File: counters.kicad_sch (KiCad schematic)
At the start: 20 parts, among them K15 Fujitsu_FTR-LYAA005x, K17 Relay_SPDT, Q293 DMP3099L, Q294 DMP3099L, Q869 2N7002, Q871 2N7002, SW1 SW_Push, SW2 SW_Push

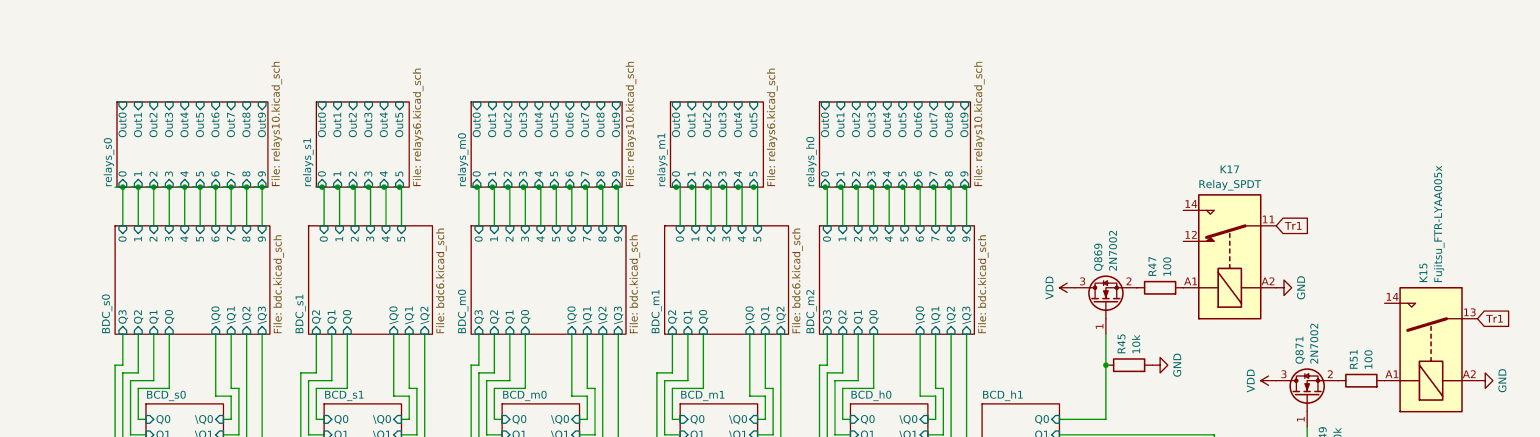
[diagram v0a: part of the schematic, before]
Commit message: moved to 3v3
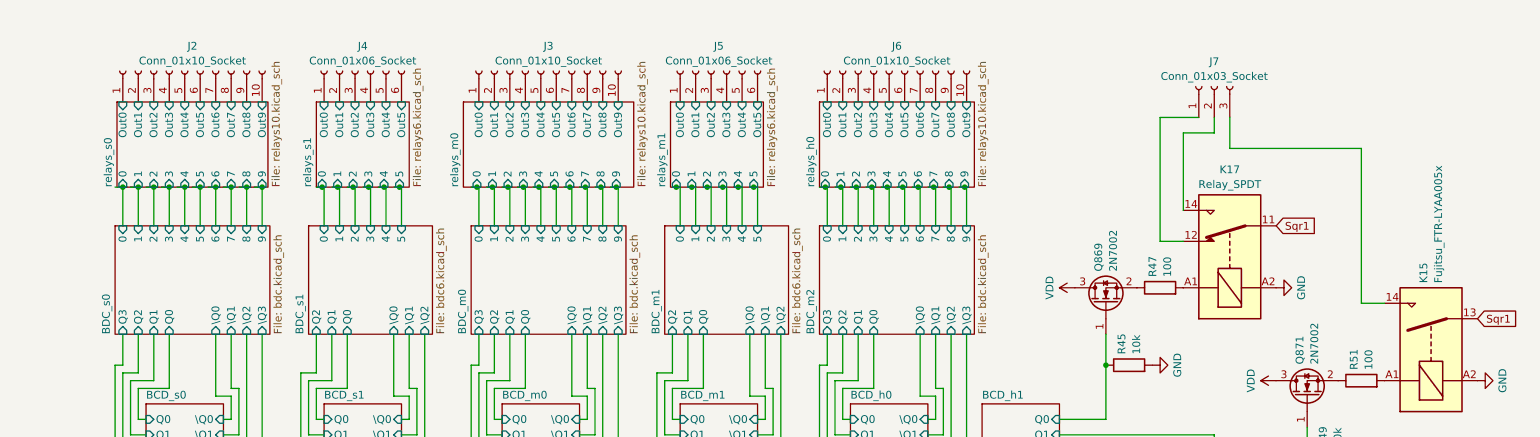
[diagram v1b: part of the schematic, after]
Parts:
- added J2, J3, J6: Conn_01x10_Socket, symbol Connector:Conn_01x10_Socket
- added J4, J5: Conn_01x06_Socket, symbol Connector:Conn_01x06_Socket
- added J7: Conn_01x03_Socket, symbol Connector:Conn_01x03_Socket
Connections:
- net relays_h0/Out0: now also J6.1 (Pin_1)
- net relays_h0/Out1: now also J6.2 (Pin_2)
- net relays_h0/Out2: now also J6.3 (Pin_3)
- net relays_h0/Out3: now also J6.4 (Pin_4)
- net relays_h0/Out4: now also J6.5 (Pin_5)
- net relays_h0/Out5: now also J6.6 (Pin_6)
- net relays_h0/Out6: now also J6.7 (Pin_7)
- net relays_h0/Out7: now also J6.8 (Pin_8)
- net relays_h0/Out8: now also J6.9 (Pin_9)
- net relays_h0/Out9: now also J6.10 (Pin_10)
- net relays_m0/Out0: now also J3.1 (Pin_1)
- net relays_m0/Out1: now also J3.2 (Pin_2)
- net relays_m0/Out2: now also J3.3 (Pin_3)
- net relays_m0/Out3: now also J3.4 (Pin_4)
- net relays_m0/Out4: now also J3.5 (Pin_5)
- net relays_m0/Out5: now also J3.6 (Pin_6)
- net relays_m0/Out6: now also J3.7 (Pin_7)
- net relays_m0/Out7: now also J3.8 (Pin_8)
- net relays_m0/Out8: now also J3.9 (Pin_9)
- net relays_m0/Out9: now also J3.10 (Pin_10)
- net relays_m1/Out0: now also J5.1 (Pin_1)
- net relays_m1/Out1: now also J5.2 (Pin_2)
- net relays_m1/Out2: now also J5.3 (Pin_3)
- net relays_m1/Out3: now also J5.4 (Pin_4)
- net relays_m1/Out4: now also J5.5 (Pin_5)
- net relays_m1/Out5: now also J5.6 (Pin_6)
- net relays_s0/Out0: now also J2.1 (Pin_1)
- net relays_s0/Out1: now also J2.2 (Pin_2)
- net relays_s0/Out2: now also J2.3 (Pin_3)
- net relays_s0/Out3: now also J2.4 (Pin_4)
- net relays_s0/Out4: now also J2.5 (Pin_5)
- net relays_s0/Out5: now also J2.6 (Pin_6)
- net relays_s0/Out6: now also J2.7 (Pin_7)
- net relays_s0/Out7: now also J2.8 (Pin_8)
- net relays_s0/Out8: now also J2.9 (Pin_9)
- net relays_s0/Out9: now also J2.10 (Pin_10)
- net relays_s1/Out0: now also J4.1 (Pin_1)
- net relays_s1/Out1: now also J4.2 (Pin_2)
- net relays_s1/Out2: now also J4.3 (Pin_3)
- net relays_s1/Out3: now also J4.4 (Pin_4)
- net relays_s1/Out4: now also J4.5 (Pin_5)
- net relays_s1/Out5: now also J4.6 (Pin_6)
- net at K15.14: now also J7.3 (Pin_3)
- net at K17.12: now also J7.1 (Pin_1)
- net at K17.14: now also J7.2 (Pin_2)
- net Tr1 renamed Sqr1

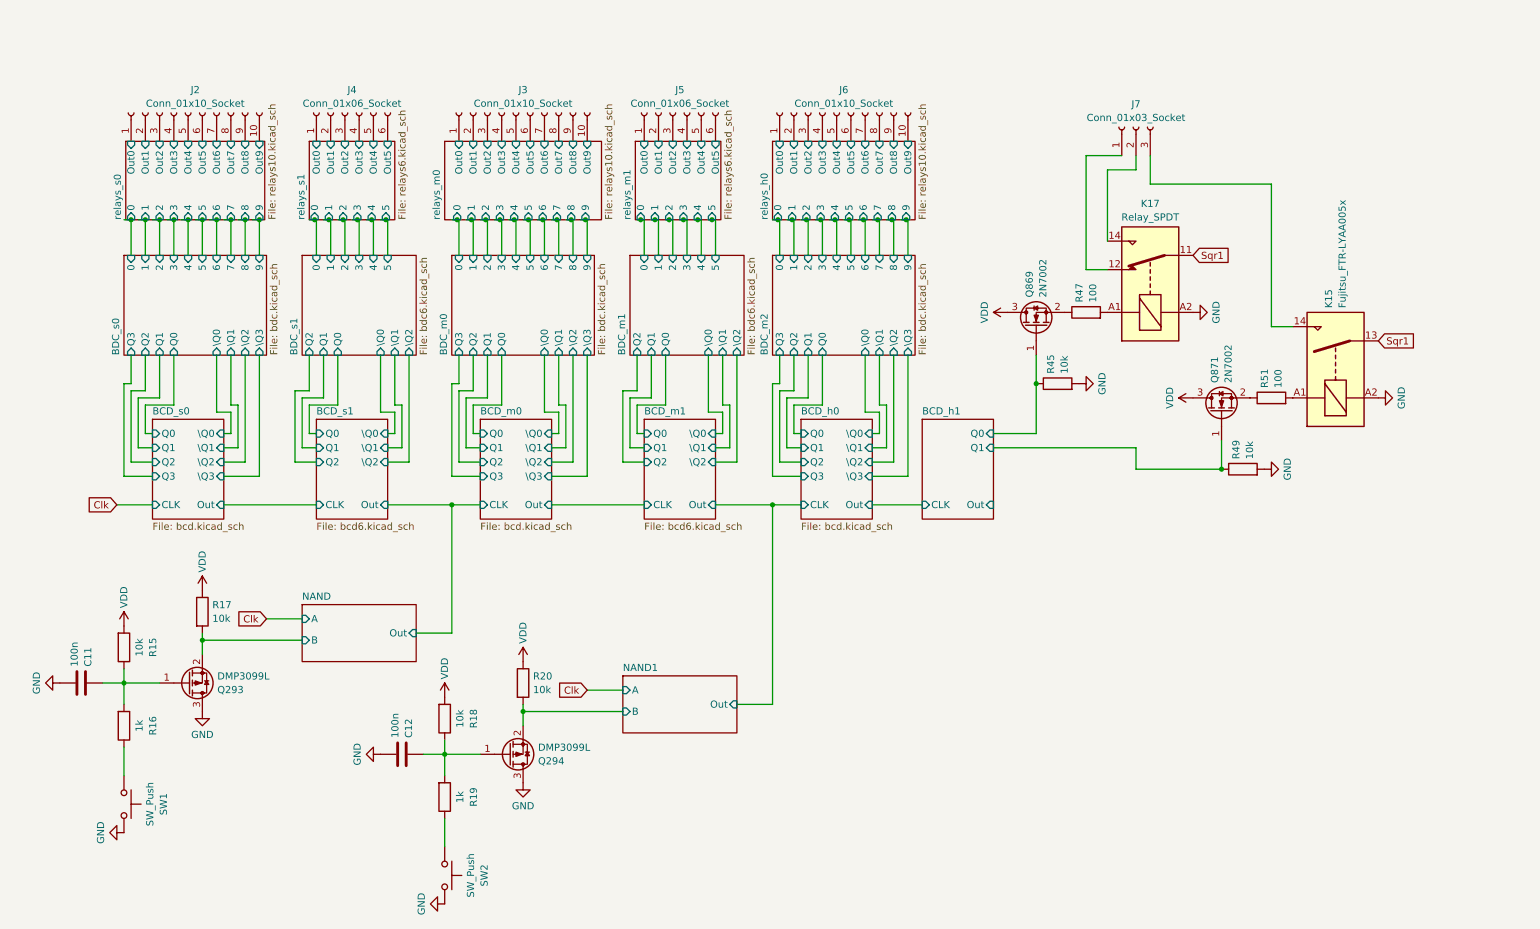
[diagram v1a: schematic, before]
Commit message: added decoupling caps
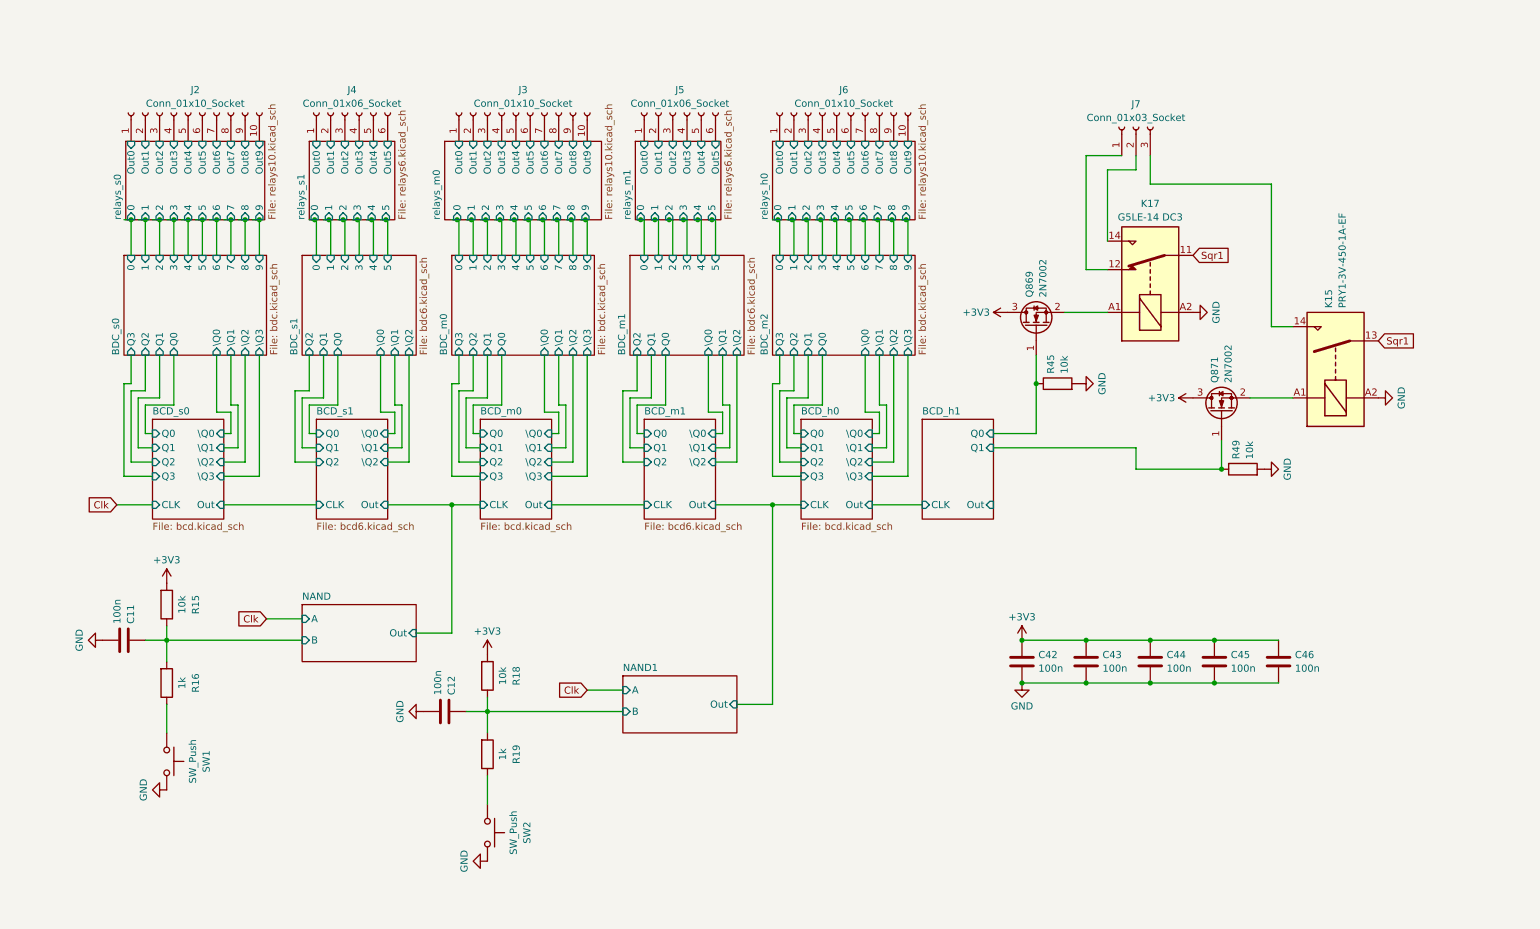
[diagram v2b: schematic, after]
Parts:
- removed Q293, Q294: DMP3099L, Package_TO_SOT_SMD:SOT-23, symbol Transistor_FET:DMP3099L
- removed R17, R20: 10k, Resistor_SMD:R_0402_1005Metric, symbol Device:R
- removed R47, R51: 100, Resistor_SMD:R_0402_1005Metric, symbol Device:R
- added C42, C43, C44, C45, C46: 100n, symbol Device:C
- K15: value Fujitsu_FTR-LYAA005x -> PRY1-3V-450-1A-EF
- K17: value Relay_SPDT -> G5LE-14 DC3
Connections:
- net GND: now also C42.2, C43.2, C44.2, C45.2, C46.2
- net NAND/B: now also C11.1, R15.1, R16.2
- net NAND1/B: now also C12.1, R18.1, R19.2
- net at K15.A1: now also Q871.2 (S)
- net at K17.A1: now also Q869.2 (S)
- net VDD renamed +3V3
- net +3V3: now also C42.1, C43.1, C44.1, C45.1, C46.1
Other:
- moved on the sheet: C11, C12, R15, R16, R18, R19, SW1, SW2

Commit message: corrected output/input type of pins
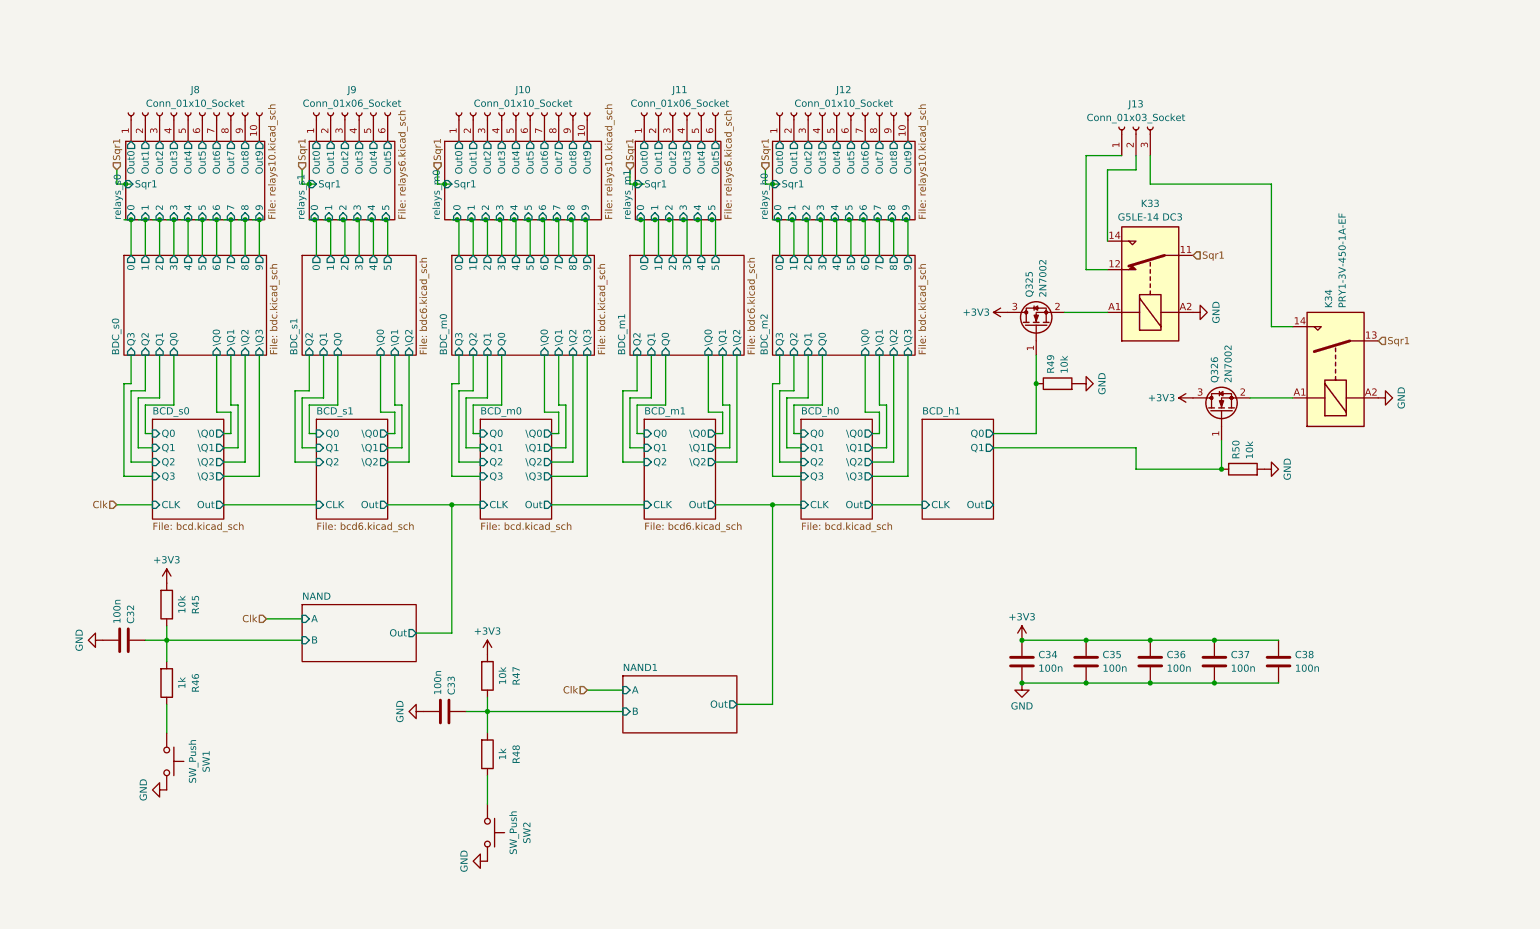
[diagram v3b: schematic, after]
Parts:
- C32: renamed from C11; footprint (none) -> Capacitor_SMD:C_0603_1608Metric
- C33: renamed from C12; footprint (none) -> Capacitor_SMD:C_0603_1608Metric
- C34: renamed from C42; footprint (none) -> Capacitor_SMD:C_0603_1608Metric
- C35: renamed from C43; footprint (none) -> Capacitor_SMD:C_0603_1608Metric
- C36: renamed from C44; footprint (none) -> Capacitor_SMD:C_0603_1608Metric
- C37: renamed from C45; footprint (none) -> Capacitor_SMD:C_0603_1608Metric
- C38: renamed from C46; footprint (none) -> Capacitor_SMD:C_0603_1608Metric
- J10: renamed from J3; footprint (none) -> Connector_PinHeader_2.54mm:PinHeader_1x10_P2.54mm_Vertical
- J11: renamed from J5; footprint (none) -> Connector_PinHeader_2.54mm:PinHeader_1x06_P2.54mm_Vertical
- J12: renamed from J6; footprint (none) -> Connector_PinHeader_2.54mm:PinHeader_1x10_P2.54mm_Vertical
- J13: renamed from J7; footprint (none) -> Connector_PinHeader_2.54mm:PinHeader_1x03_P2.54mm_Vertical
- J8: renamed from J2; footprint (none) -> Connector_PinHeader_2.54mm:PinHeader_1x10_P2.54mm_Vertical
- J9: renamed from J4; footprint (none) -> Connector_PinHeader_2.54mm:PinHeader_1x06_P2.54mm_Vertical
- K33: renamed from K17; footprint (none) -> Relay_THT:Relay_SPDT_Omron-G5LE-1
- K34: renamed from K15; footprint Relay_THT:Relay_SPST-NO_Fujitsu_FTR-LYAA005x_FormA_Vertical -> Relay_THT:Relay_SPST_Omron_G5PZ
- SW1, SW2: footprint (none) -> Button_Switch_SMD:SW_Push_1P1T_NO_CK_PTS125Sx43PSMTR
- renumbered Q869 to Q325, Q871 to Q326, R15 to R45, R16 to R46, R18 to R47, R19 to R48, R45 to R49, R49 to R50
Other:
- sheet relays_h0 ports: added Sqr1; removed none
- sheet relays_m0 ports: added Sqr1; removed none
- sheet relays_m1 ports: added Sqr1; removed none
- sheet relays_s0 ports: added Sqr1; removed none
- sheet relays_s1 ports: added Sqr1; removed none

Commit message: schematic cleanup, routed 1 bdc
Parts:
- removed K33: G5LE-14 DC3, Relay_THT:Relay_SPDT_Omron-G5LE-1, symbol Relay:Relay_SPDT
- removed K34: PRY1-3V-450-1A-EF, Relay_THT:Relay_SPST_Omron_G5PZ, symbol Relay:Fujitsu_FTR-LYAA005x
- removed Q325, Q326: 2N7002, Package_TO_SOT_SMD:SOT-23, symbol Transistor_FET:2N7002
- removed R49, R50: 10k, Resistor_SMD:R_0402_1005Metric, symbol Device:R
- added Q591: DMP3099L, Package_TO_SOT_SMD:SOT-23, symbol Transistor_FET:DMP3099L
- added Q592: 2N7002, Package_TO_SOT_SMD:SOT-23, symbol Transistor_FET:2N7002
- renumbered C32 to C38, C33 to C39, C34 to C40, C35 to C41, C36 to C42, C37 to C43, C38 to C44, R45 to R13, R46 to R14, R47 to R15, R48 to R16
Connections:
- net +3V3: now also Q591.2 (S)
- net BCD_h1/Q0: now also Q591.1 (G), Q592.1 (G)
- net GND: now also Q592.2 (S)
- net SSR/AC1: now reaches J13.3 (Pin_3)
- net SSR2/AC1: now reaches J13.1 (Pin_1)
- net SSR1/AC1: now reaches J13.2 (Pin_2)
- new net SSR1/Ctrl: Q591.3 (D), Q592.3 (D)
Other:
- sheet BDC_m2 renamed BDC_h0
- added sheet SSR (ssr.kicad_sch)
- added sheet SSR1 (ssr.kicad_sch)
- added sheet SSR2 (ssr.kicad_sch)
- sheet NAND: file and.kicad_sch -> nand.kicad_sch
- sheet NAND1: file and.kicad_sch -> nand.kicad_sch
- moved on the sheet: J13
